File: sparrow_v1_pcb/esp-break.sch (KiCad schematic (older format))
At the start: 43 parts, among them J1 Conn_02x03_Odd_Even, J4 Conn_01x01, Q1 BSS138, Q2 BSS138, Q3_F1 BSS138, SW1 SW_Push, U1 ESP32-WROOM-32, U2 AP1117-33

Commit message: Minor trace modification and checked by Ovee. Updated the footprints in the schematics as well
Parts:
- C1, C2, C3, C4, C5, C6: footprint Capacitor_SMD:C_1206_3216Metric -> Capacitor_SMD:C_0201_0603Metric
- D1: footprint LED_SMD:LED_1206_3216Metric -> LED_SMD:LED_0603_1608Metric
- R1, R2, R3, R4, R5, R6, RF1, RF12, RF2, RF3, RF4, RF5, RF6, RF7, RF8, RF9, RS10, RS11, RS14, RS3, RS4, RS6, RS7, RS8: footprint Resistor_SMD:R_1206_3216Metric -> Resistor_SMD:R_0603_1608Metric
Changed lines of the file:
@@
 F 0 "C2" H 6578 3146 50  0000 L CNN
 F 1 "0.1uf" H 6578 3055 50  0000 L CNN
-F 2 "Capacitor_SMD:C_1206_3216Metric" H 6400 3100 50  0001 C CNN
+F 2 "Capacitor_SMD:C_0201_0603Metric" H 6400 3100 50  0001 C CNN
 F 3 "~" H 6400 3100 50  0001 C CNN
 	1    6400 3100
@@
 F 0 "C1" H 6128 3146 50  0000 L CNN
 F 1 "22uf" H 6128 3055 50  0000 L CNN
-F 2 "Capacitor_SMD:C_1206_3216Metric" H 5950 3100 50  0001 C CNN
+F 2 "Capacitor_SMD:C_0201_0603Metric" H 5950 3100 50  0001 C CNN
 F 3 "~" H 5950 3100 50  0001 C CNN
 	1    5950 3100
@@
 F 0 "C4" H 7878 3146 50  0000 L CNN
 F 1 "22uf" H 7878 3055 50  0000 L CNN
-F 2 "Capacitor_SMD:C_1206_3216Metric" H 7700 3100 50  0001 C CNN
+F 2 "Capacitor_SMD:C_0201_0603Metric" H 7700 3100 50  0001 C CNN
 F 3 "~" H 7700 3100 50  0001 C CNN
 	1    7700 3100
@@
 F 0 "C3" H 7428 3146 50  0000 L CNN
 F 1 "0.1uf" H 7428 3055 50  0000 L CNN
-F 2 "Capacitor_SMD:C_1206_3216Metric" H 7250 3100 50  0001 C CNN
+F 2 "Capacitor_SMD:C_0201_0603Metric" H 7250 3100 50  0001 C CNN
 F 3 "~" H 7250 3100 50  0001 C CNN
 	1    7250 3100
@@
 F 0 "R1" H 4370 4396 50  0000 L CNN
 F 1 "10k" H 4370 4305 50  0000 L CNN
-F 2 "Resistor_SMD:R_1206_3216Metric" V 4230 4350 50  0001 C CNN
+F 2 "Resistor_SMD:R_0603_1608Metric" V 4230 4350 50  0001 C CNN
 F 3 "~" H 4300 4350 50  0001 C CNN
 	1    4300 4350
@@
 F 0 "D1" H 4593 2395 50  0000 C CNN
 F 1 "LED" H 4593 2486 50  0000 C CNN
-F 2 "LED_SMD:LED_1206_3216Metric" H 4600 2650 50  0001 C CNN
+F 2 "LED_SMD:LED_0603_1608Metric" H 4600 2650 50  0001 C CNN
 F 3 "~" H 4600 2650 50  0001 C CNN
 	1    4600 2650
@@
 F 0 "RS6" H 9320 3996 50  0000 L CNN
 F 1 "0" H 9320 3905 50  0000 L CNN
-F 2 "Resistor_SMD:R_1206_3216Metric" V 9180 3950 50  0001 C CNN
+F 2 "Resistor_SMD:R_0603_1608Metric" V 9180 3950 50  0001 C CNN
 F 3 "~" H 9250 3950 50  0001 C CNN
 	1    9250 3950
@@
 F 0 "RF9" H 9620 3696 50  0000 L CNN
 F 1 "0" H 9620 3605 50  0000 L CNN
-F 2 "Resistor_SMD:R_1206_3216Metric" V 9480 3650 50  0001 C CNN
+F 2 "Resistor_SMD:R_0603_1608Metric" V 9480 3650 50  0001 C CNN
 F 3 "~" H 9550 3650 50  0001 C CNN
 	1    9550 3650
@@
 F 0 "RS11" H 9920 3996 50  0000 L CNN
 F 1 "0" H 9920 3905 50  0000 L CNN
-F 2 "Resistor_SMD:R_1206_3216Metric" V 9780 3950 50  0001 C CNN
+F 2 "Resistor_SMD:R_0603_1608Metric" V 9780 3950 50  0001 C CNN
 F 3 "~" H 9850 3950 50  0001 C CNN
 	1    9850 3950
@@
 F 0 "RS8" H 9620 3496 50  0000 L CNN
 F 1 "0" H 9620 3405 50  0000 L CNN
-F 2 "Resistor_SMD:R_1206_3216Metric" V 9480 3450 50  0001 C CNN
+F 2 "Resistor_SMD:R_0603_1608Metric" V 9480 3450 50  0001 C CNN
 F 3 "~" H 9550 3450 50  0001 C CNN
 	1    9550 3450
@@
 F 0 "RF5" H 8970 3496 50  0000 L CNN
 F 1 "0" H 8970 3405 50  0000 L CNN
-F 2 "Resistor_SMD:R_1206_3216Metric" V 8830 3450 50  0001 C CNN
+F 2 "Resistor_SMD:R_0603_1608Metric" V 8830 3450 50  0001 C CNN
 F 3 "~" H 8900 3450 50  0001 C CNN
 	1    8900 3450
@@
 F 0 "RF12" H 10270 3496 50  0000 L CNN
 F 1 "0" H 10270 3405 50  0000 L CNN
-F 2 "Resistor_SMD:R_1206_3216Metric" V 10130 3450 50  0001 C CNN
+F 2 "Resistor_SMD:R_0603_1608Metric" V 10130 3450 50  0001 C CNN
 F 3 "~" H 10200 3450 50  0001 C CNN
 	1    10200 3450
@@
 F 0 "RF7" H 9570 2946 50  0000 L CNN
 F 1 "0" H 9570 2855 50  0000 L CNN
-F 2 "Resistor_SMD:R_1206_3216Metric" V 9430 2900 50  0001 C CNN
+F 2 "Resistor_SMD:R_0603_1608Metric" V 9430 2900 50  0001 C CNN
 F 3 "~" H 9500 2900 50  0001 C CNN
 	1    9500 2900
@@
 F 0 "RS10" H 9450 2950 50  0000 L CNN
 F 1 "0" H 9500 2850 50  0000 L CNN
-F 2 "Resistor_SMD:R_1206_3216Metric" V 9530 2900 50  0001 C CNN
+F 2 "Resistor_SMD:R_0603_1608Metric" V 9530 2900 50  0001 C CNN
 F 3 "~" H 9600 2900 50  0001 C CNN
 	1    9600 2900
@@
 F 0 "RS3" H 8870 3796 50  0000 L CNN
 F 1 "220k" H 8870 3705 50  0000 L CNN
-F 2 "Resistor_SMD:R_1206_3216Metric" V 8730 3750 50  0001 C CNN
+F 2 "Resistor_SMD:R_0603_1608Metric" V 8730 3750 50  0001 C CNN
 F 3 "~" H 8800 3750 50  0001 C CNN
 	1    8800 3750
@@
 F 0 "RS4" H 8870 4196 50  0000 L CNN
 F 1 "120k" H 8870 4105 50  0000 L CNN
-F 2 "Resistor_SMD:R_1206_3216Metric" V 8730 4150 50  0001 C CNN
+F 2 "Resistor_SMD:R_0603_1608Metric" V 8730 4150 50  0001 C CNN
 F 3 "~" H 8800 4150 50  0001 C CNN
 	1    8800 4150
@@
 F 0 "C5" H 4478 3996 50  0000 L CNN
 F 1 "0.1uf" H 4478 3905 50  0000 L CNN
-F 2 "Capacitor_SMD:C_1206_3216Metric" H 4300 3950 50  0001 C CNN
+F 2 "Capacitor_SMD:C_0201_0603Metric" H 4300 3950 50  0001 C CNN
 F 3 "~" H 4300 3950 50  0001 C CNN
 	1    4300 3950
@@
 F 0 "R2" H 4370 2696 50  0000 L CNN
 F 1 "330" H 4370 2605 50  0000 L CNN
-F 2 "Resistor_SMD:R_1206_3216Metric" V 4230 2650 50  0001 C CNN
+F 2 "Resistor_SMD:R_0603_1608Metric" V 4230 2650 50  0001 C CNN
 F 3 "~" H 4300 2650 50  0001 C CNN
 	1    4300 2650
@@
 F 0 "C6" H 4978 4496 50  0000 L CNN
 F 1 "0.1uf" H 4978 4405 50  0000 L CNN
-F 2 "Capacitor_SMD:C_1206_3216Metric" H 4800 4450 50  0001 C CNN
+F 2 "Capacitor_SMD:C_0201_0603Metric" H 4800 4450 50  0001 C CNN
 F 3 "~" H 4800 4450 50  0001 C CNN
 	1    4800 4450
@@
 F 0 "R3" H 5770 1046 50  0000 L CNN
 F 1 "10k" H 5770 955 50  0000 L CNN
-F 2 "Resistor_SMD:R_1206_3216Metric" V 5630 1000 50  0001 C CNN
+F 2 "Resistor_SMD:R_0603_1608Metric" V 5630 1000 50  0001 C CNN
 F 3 "~" H 5700 1000 50  0001 C CNN
 	1    5700 1000
@@
 F 0 "R4" H 6270 1046 50  0000 L CNN
 F 1 "10k" H 6270 955 50  0000 L CNN
-F 2 "Resistor_SMD:R_1206_3216Metric" V 6130 1000 50  0001 C CNN
+F 2 "Resistor_SMD:R_0603_1608Metric" V 6130 1000 50  0001 C CNN
 F 3 "~" H 6200 1000 50  0001 C CNN
 	1    6200 1000
@@
 F 0 "RS7" H 5770 1596 50  0000 L CNN
 F 1 "0" H 5770 1505 50  0000 L CNN
-F 2 "Resistor_SMD:R_1206_3216Metric" V 5630 1550 50  0001 C CNN
+F 2 "Resistor_SMD:R_0603_1608Metric" V 5630 1550 50  0001 C CNN
 F 3 "~" H 5700 1550 50  0001 C CNN
 	1    5700 1550
@@
 F 0 "RF2" V 5400 1400 50  0000 L CNN
 F 1 "0" H 5400 1350 50  0000 L CNN
-F 2 "Resistor_SMD:R_1206_3216Metric" V 5430 1350 50  0001 C CNN
+F 2 "Resistor_SMD:R_0603_1608Metric" V 5430 1350 50  0001 C CNN
 F 3 "~" H 5500 1350 50  0001 C CNN
 	1    5500 1350
@@
 F 0 "R5" H 7420 1046 50  0000 L CNN
 F 1 "10k" H 7420 955 50  0000 L CNN
-F 2 "Resistor_SMD:R_1206_3216Metric" V 7280 1000 50  0001 C CNN
+F 2 "Resistor_SMD:R_0603_1608Metric" V 7280 1000 50  0001 C CNN
 F 3 "~" H 7350 1000 50  0001 C CNN
 	1    7350 1000
@@
 F 0 "R6" H 7920 1046 50  0000 L CNN
 F 1 "10k" H 7920 955 50  0000 L CNN
-F 2 "Resistor_SMD:R_1206_3216Metric" V 7780 1000 50  0001 C CNN
+F 2 "Resistor_SMD:R_0603_1608Metric" V 7780 1000 50  0001 C CNN
 F 3 "~" H 7850 1000 50  0001 C CNN
 	1    7850 1000
@@
 F 0 "RS14" H 7420 1596 50  0000 L CNN
 F 1 "0" H 7420 1505 50  0000 L CNN
-F 2 "Resistor_SMD:R_1206_3216Metric" V 7280 1550 50  0001 C CNN
+F 2 "Resistor_SMD:R_0603_1608Metric" V 7280 1550 50  0001 C CNN
 F 3 "~" H 7350 1550 50  0001 C CNN
 	1    7350 1550
@@
 F 0 "RF3" V 7050 1400 50  0000 L CNN
 F 1 "0" H 7050 1350 50  0000 L CNN
-F 2 "Resistor_SMD:R_1206_3216Metric" V 7080 1350 50  0001 C CNN
+F 2 "Resistor_SMD:R_0603_1608Metric" V 7080 1350 50  0001 C CNN
 F 3 "~" H 7150 1350 50  0001 C CNN
 	1    7150 1350
@@
 F 0 "RF4" H 8920 1046 50  0000 L CNN
 F 1 "10k" H 8920 955 50  0000 L CNN
-F 2 "Resistor_SMD:R_1206_3216Metric" V 8780 1000 50  0001 C CNN
+F 2 "Resistor_SMD:R_0603_1608Metric" V 8780 1000 50  0001 C CNN
 F 3 "~" H 8850 1000 50  0001 C CNN
 	1    8850 1000
@@
 F 0 "RF6" H 9420 1046 50  0000 L CNN
 F 1 "10k" H 9420 955 50  0000 L CNN
-F 2 "Resistor_SMD:R_1206_3216Metric" V 9280 1000 50  0001 C CNN
+F 2 "Resistor_SMD:R_0603_1608Metric" V 9280 1000 50  0001 C CNN
 F 3 "~" H 9350 1000 50  0001 C CNN
 	1    9350 1000
@@
 F 0 "RF8" H 8920 1596 50  0000 L CNN
 F 1 "0" H 8920 1505 50  0000 L CNN
-F 2 "Resistor_SMD:R_1206_3216Metric" V 8780 1550 50  0001 C CNN
+F 2 "Resistor_SMD:R_0603_1608Metric" V 8780 1550 50  0001 C CNN
 F 3 "~" H 8850 1550 50  0001 C CNN
 	1    8850 1550
@@
 F 0 "RF1" H 10320 3596 50  0000 L CNN
 F 1 "0" H 10320 3505 50  0000 L CNN
-F 2 "Resistor_SMD:R_1206_3216Metric" V 10180 3550 50  0001 C CNN
+F 2 "Resistor_SMD:R_0603_1608Metric" V 10180 3550 50  0001 C CNN
 F 3 "~" H 10250 3550 50  0001 C CNN
 	1    10250 3550

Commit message: Updated schematics and pcbnew with updated components and removed unnecessary components
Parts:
- removed J4: Conn_01x01, Connector:Banana_Jack_1Pin, symbol Connector_Generic:Conn_01x01
- removed RF1, RF12, RF2, RF3, RF5, RF7, RF8, RF9, RS10, RS11, RS14, RS6, RS7, RS8: 0, Resistor_SMD:R_0603_1608Metric, symbol Device:R
- removed RS3: 220k, Resistor_SMD:R_0603_1608Metric, symbol Device:R
- removed RS4: 120k, Resistor_SMD:R_0603_1608Metric, symbol Device:R
- D1: footprint LED_SMD:LED_0603_1608Metric -> LED_SMD:LED_0201_0603Metric
- PWR2: footprint Connector_USB:USB_Micro-B_Molex_47346-0001 -> Connector_USB:USB_Micro-B_Molex-105017-0001
- R1, R2, R3, R4, R5, R6, RF4, RF6: footprint Resistor_SMD:R_0603_1608Metric -> Resistor_SMD:R_0201_0603Metric
- U1: value ESP32-WROOM-32 -> ESP32-WROOM-32D; symbol RF_Module:ESP32-WROOM-32 -> RF_Module:ESP32-WROOM-32D
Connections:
- net 5_c1: now also IN1.4 (Pin_4)
- net 5_c2: now also OUT1.4 (Pin_4)
- net 5_c3: now also IN1.5 (Pin_5), OUT1.5 (Pin_5)
- net RX2: now also Q1.2 (S), R3.2
- net TX2: now also Q2.2 (S), R5.2
- net gnd: now also IN1.2 (Pin_2), OUT1.2 (Pin_2)
- net rx: now also Q3_F1.2 (S), RF4.2
- net at OUT1.6 (Pin_6): now also IN1.6 (Pin_6)
- net adc0: no longer names the net of U1.4 (SENSOR_VP)
- net adc3: no longer names the net of U1.5 (SENSOR_VN)
- net adc4: no longer names the net of U1.8 (IO32)
- net adc5: no longer names the net of U1.9 (IO33)
- net io13: no longer names the net of U1.16 (IO13)
- net io19: no longer names the net of U1.31 (IO19)
- net io21: no longer names the net of U1.33 (IO21)
- net io23: no longer names the net of U1.37 (IO23)
- net io25: no longer names the net of U1.10 (IO25)
- net io26: no longer names the net of U1.11 (IO26)
- net io27: no longer names the net of U1.12 (IO27)
- net touch: no longer names the net of U1.26 (IO4)
- no-connect marks 0 -> 30

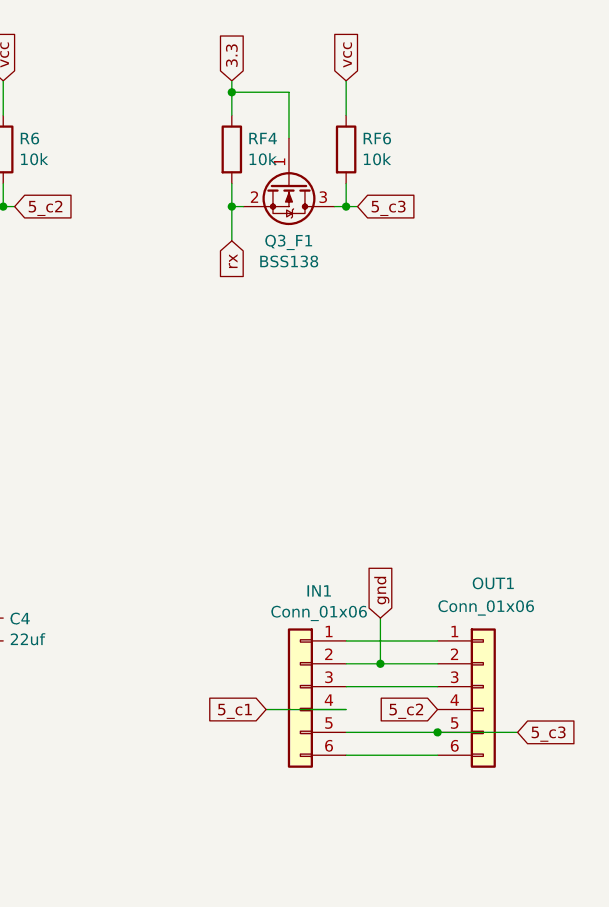
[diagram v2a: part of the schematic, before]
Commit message: removed rx line from 5th pin
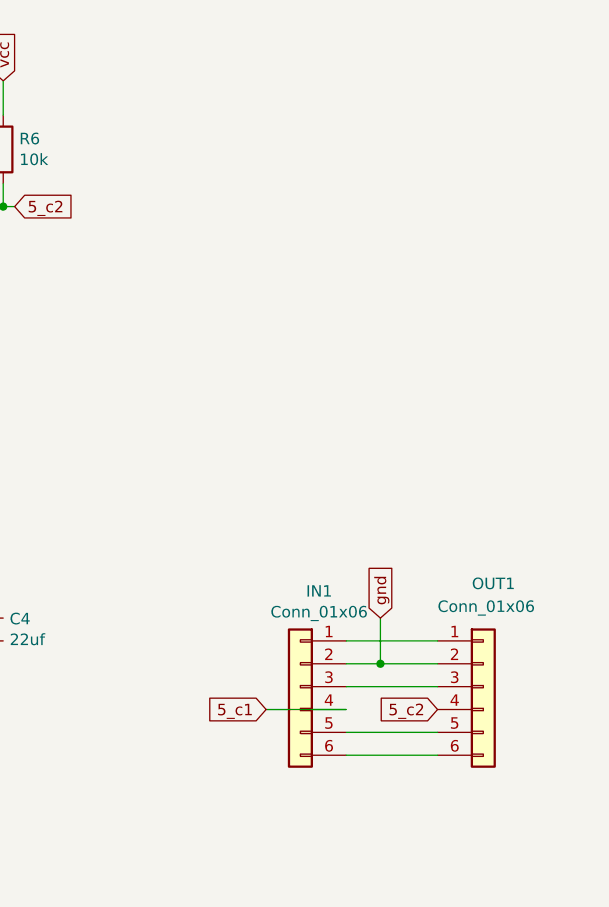
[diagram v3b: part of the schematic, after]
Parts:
- removed Q3_F1: BSS138, Package_TO_SOT_SMD:SOT-23, symbol Transistor_FET:BSS138
- removed RF4, RF6: 10k, Resistor_SMD:R_0201_0603Metric, symbol Device:R
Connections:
- net 5_c3: no longer names the net of IN1.5 (Pin_5), OUT1.5 (Pin_5)
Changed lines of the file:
@@
 Text GLabel 9750 3450 0    50   Input ~ 0
 5_c2
-$Comp
-L Transistor_FET:BSS138 Q3_F1
-U 1 1 5DF0C0EF
-P 9100 1150
-F 0 "Q3_F1" V 9351 1150 50  0000 C CNN
-F 1 "BSS138" V 9442 1150 50  0000 C CNN
-F 2 "Package_TO_SOT_SMD:SOT-23" H 9300 1075 50  0001 L CIN
-F 3 "https://www.fairchildsemi.com/datasheets/BS/BSS138.pdf" H 9100 1150 50  0001 L CNN
-	1    9100 1150
-	0    1    1    0
-$EndComp
-$Comp
-L Device:R RF4
-U 1 1 5DF0C0F5
-P 8850 1000
-F 0 "RF4" H 8920 1046 50  0000 L CNN
-F 1 "10k" H 8920 955 50  0000 L CNN
-F 2 "Resistor_SMD:R_0201_0603Metric" V 8780 1000 50  0001 C CNN
-F 3 "~" H 8850 1000 50  0001 C CNN
-	1    8850 1000
-	1    0    0    -1
-$EndComp
-$Comp
-L Device:R RF6
-U 1 1 5DF0C0FB
-P 9350 1000
-F 0 "RF6" H 9420 1046 50  0000 L CNN
-F 1 "10k" H 9420 955 50  0000 L CNN
-F 2 "Resistor_SMD:R_0201_0603Metric" V 9280 1000 50  0001 C CNN
-F 3 "~" H 9350 1000 50  0001 C CNN
-	1    9350 1000
-	1    0    0    -1
-$EndComp
-Wire Wire Line
-	9100 950  9100 750
-Wire Wire Line
-	9100 750  8850 750
-Wire Wire Line
-	8850 750  8850 850
-Wire Wire Line
-	8850 1150 8850 1250
-Wire Wire Line
-	8850 1250 8900 1250
-Wire Wire Line
-	9300 1250 9350 1250
-Wire Wire Line
-	9350 1250 9350 1150
-Text GLabel 9350 700  1    50   Input ~ 0
-vcc
-Text GLabel 8850 700  1    50   Input ~ 0
-3.3
-Wire Wire Line
-	8850 700  8850 750
-Connection ~ 8850 750
-Wire Wire Line
-	9350 700  9350 850
-Wire Wire Line
-	9400 1250 9350 1250
-Connection ~ 9350 1250
-Connection ~ 8850 1250
-Text GLabel 9400 1250 2    50   Input ~ 0
-5_c3
-Wire Wire Line
-	8850 1250 8850 1400
-Text GLabel 8850 1400 3    50   Input ~ 0
-rx
-Text GLabel 10100 3550 2    50   Input ~ 0
-5_c3
-Wire Wire Line
-	10100 3550 9750 3550
-Connection ~ 9750 3550
 Wire Wire Line
 	9350 3150 9750 3150
